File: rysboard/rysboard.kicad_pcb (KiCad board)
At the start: 4 copper layers, 56 x 65 mm, 150 parts, among them IC1 LM74801QDRRRQ1, IC2 LM74801QDRRRQ1, J1 RPi4, J10 ToF1, J11 ToF2, J12 ToF3, J13 ToF4, J15 ToF5, J16 ToF6, J19 Fan_Connector, J2 Motor L, J20 Power_SW, J22 CH1_T, J23 CH2_T, J3 Motor R, J4 Cell3, J5 Cell2, J6 Cell1, J7 Conn_01x02, J9 IMU, Q1 PMV28XPEAR, Q10 PMV28XPEAR, Q11 PMV28XPEAR, Q2 FDG6304P, Q3 NST847BDP6T5G, Q5 DMP3036SSD-13, Q6 Si7938DP-T1-GE3, Q7 NST847BDP6T5G, Q9 Si7938DP-T1-GE3, U1 L6470, U2 L6470, U3 ST1S10, U4 STM32G031K8Ux, U5 74HC2G00, U6 AP7381-33SA-7, U7 AP7381-33SA-7, U9 INA181

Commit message: layers stiched
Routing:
- net GND: vias 10 -> 210
- added copper zone on In1.Cu, net GND

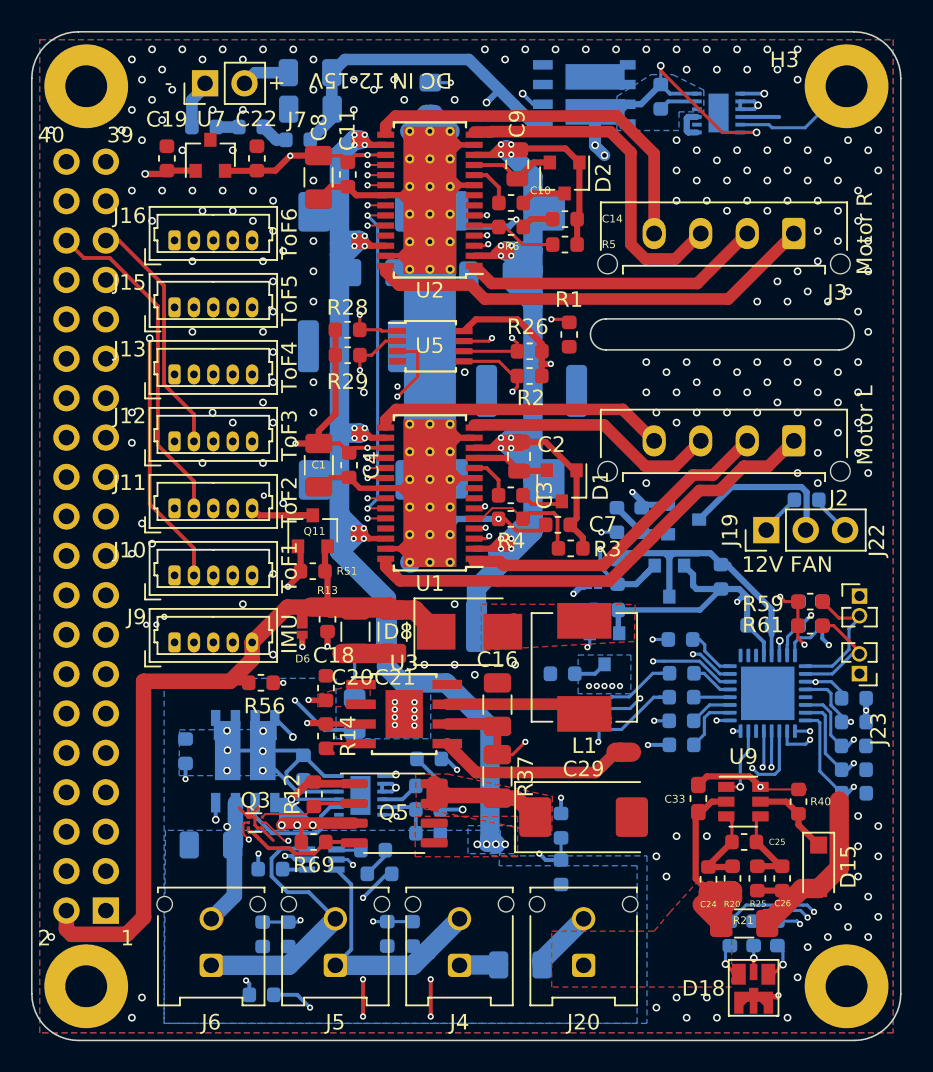
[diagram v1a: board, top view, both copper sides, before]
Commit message: Fixed regulator footprint
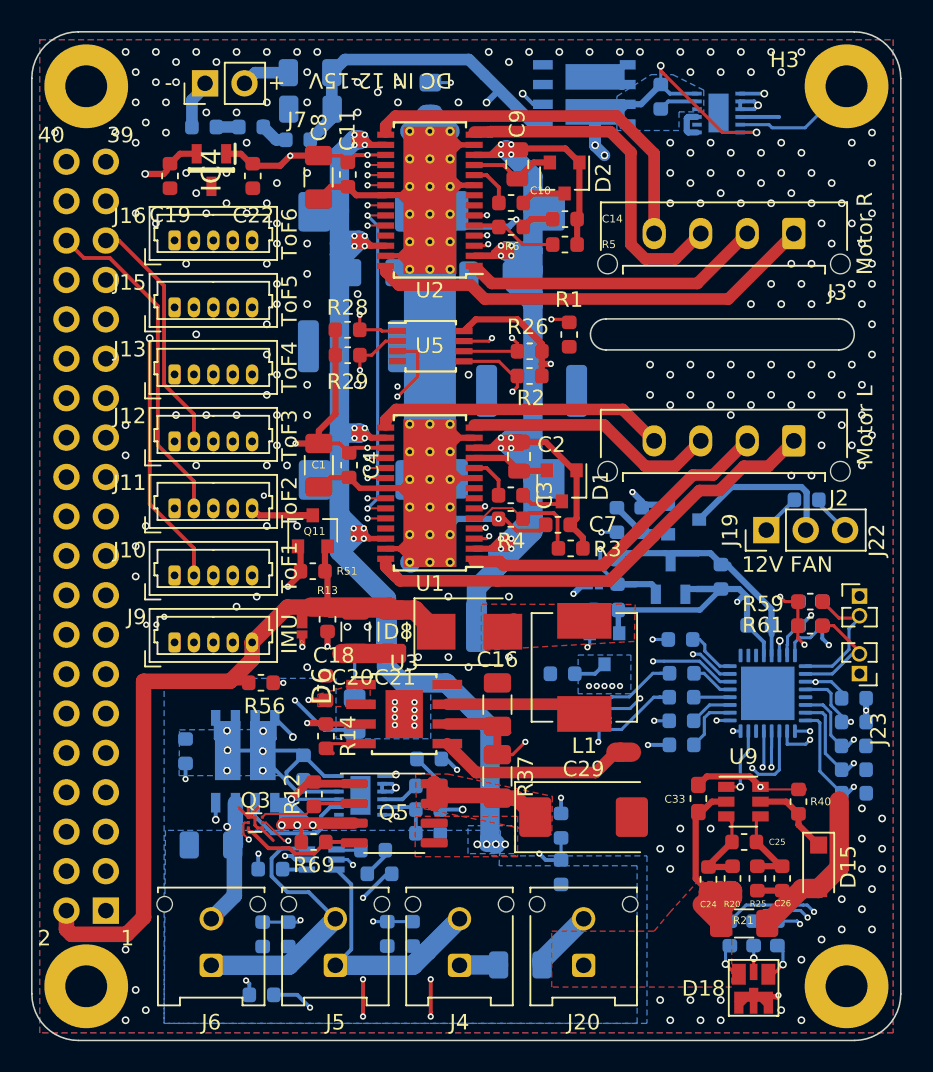
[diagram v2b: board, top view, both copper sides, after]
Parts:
- removed U6, U7: AP7381-33SA-7, Package_TO_SOT_SMD:SOT-23
- added IC3: MCP1812AT-033_TT, SOT95P237X112-3N, B.Cu at (116.5, 100.8)
- added IC4: MCP1812AT-033_TT, SOT95P237X112-3N, F.Cu at (86.9, 74.5)
- D5, D6: footprint SamacSys_Parts:DSN2_1 -> DSN2_1
- moved C22 1.16 mm to (89.5, 74.9), turned to 270 degrees
- moved C19 1.15 mm to (84.2, 74.9), turned to 270 degrees
- moved D5 0.06 mm to (111.3, 101.2)
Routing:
- net GND: track 190.8 -> 187.9 mm, vias 210 -> 220

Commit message: added connector for switch
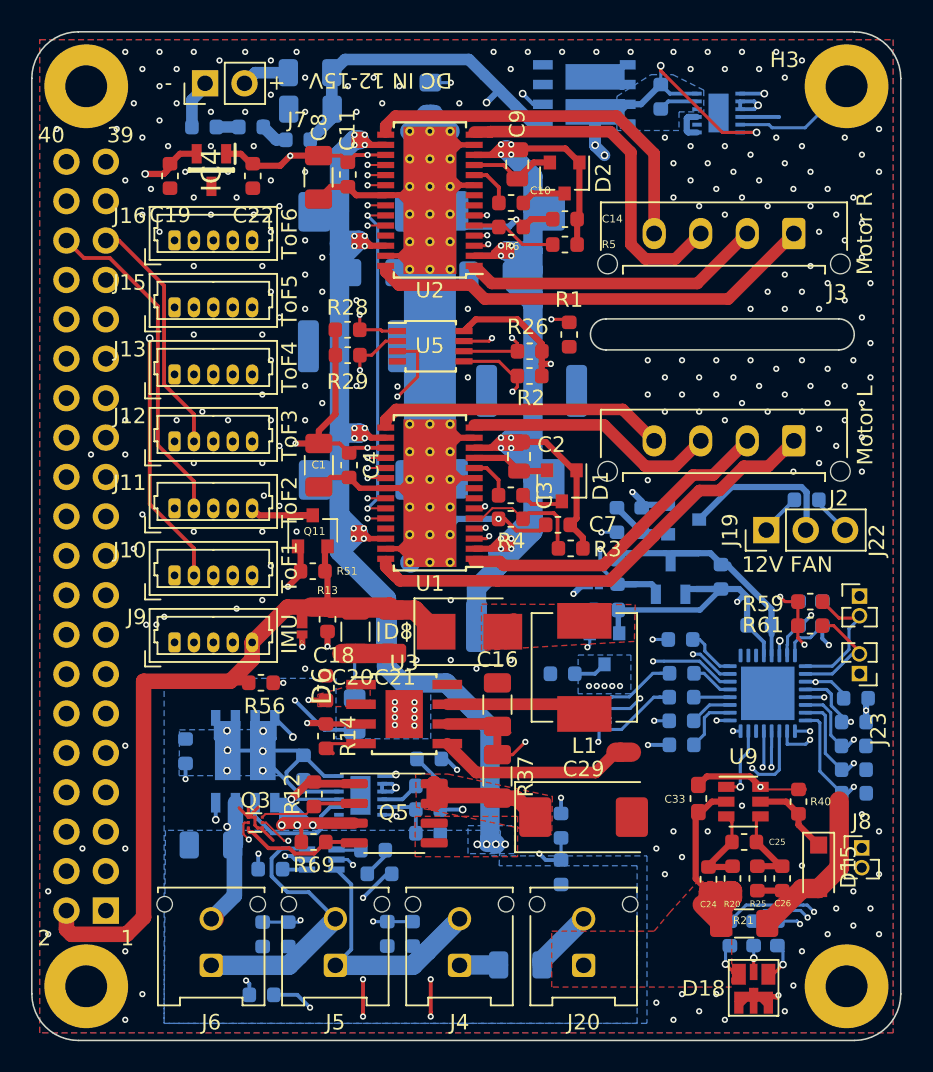
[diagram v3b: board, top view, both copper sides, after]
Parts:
- added J8: POWER SW, Connector_PinHeader_1.27mm:PinHeader_1x02_P1.27mm_Vertical, F.Cu at (128.8, 118.2)
- moved R55 0.13 mm to (128.4, 108.6)
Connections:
- U4 pad 13: /V_AUX -> /POWER_SW
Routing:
- net /POWER_SW: track 0.00 -> 15.0 mm, vias 0 -> 1
- net /BOARD_TEMP_PROBE_2: track 72.5 -> 76.3 mm
- net +5V: track 116.2 -> 117.0 mm
- net GND: vias 220 -> 226

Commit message: Bionik Logo added
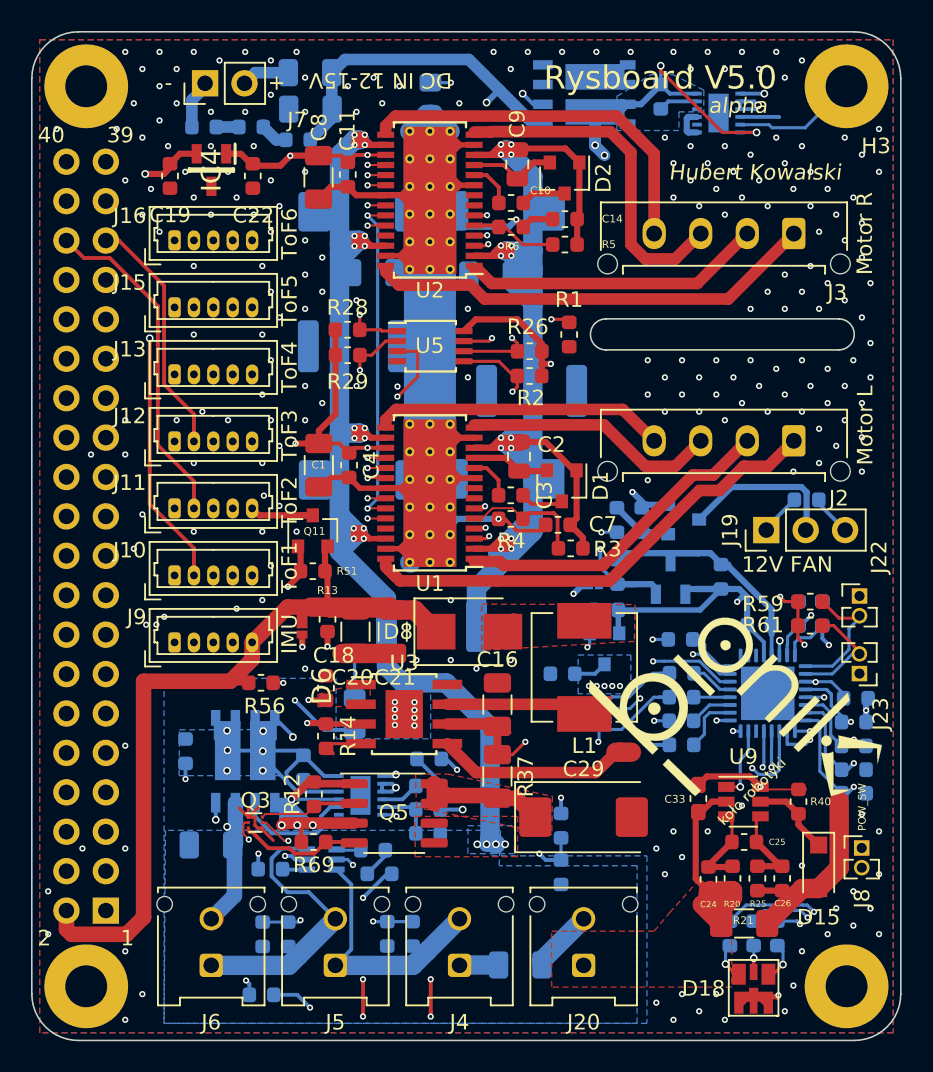
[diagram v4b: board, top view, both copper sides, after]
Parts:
- added LOGO1: bionik_logo, rysboard:bionik_logo, F.Cu at (120.6, 109.9)
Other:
- board text added: "Hubert Kowalski"
- board text added: "POW_SW"
- board text added: "Rysboard V5.0"
- board text added: "alpha"

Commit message: some acid pits fixed some ground problems fixed
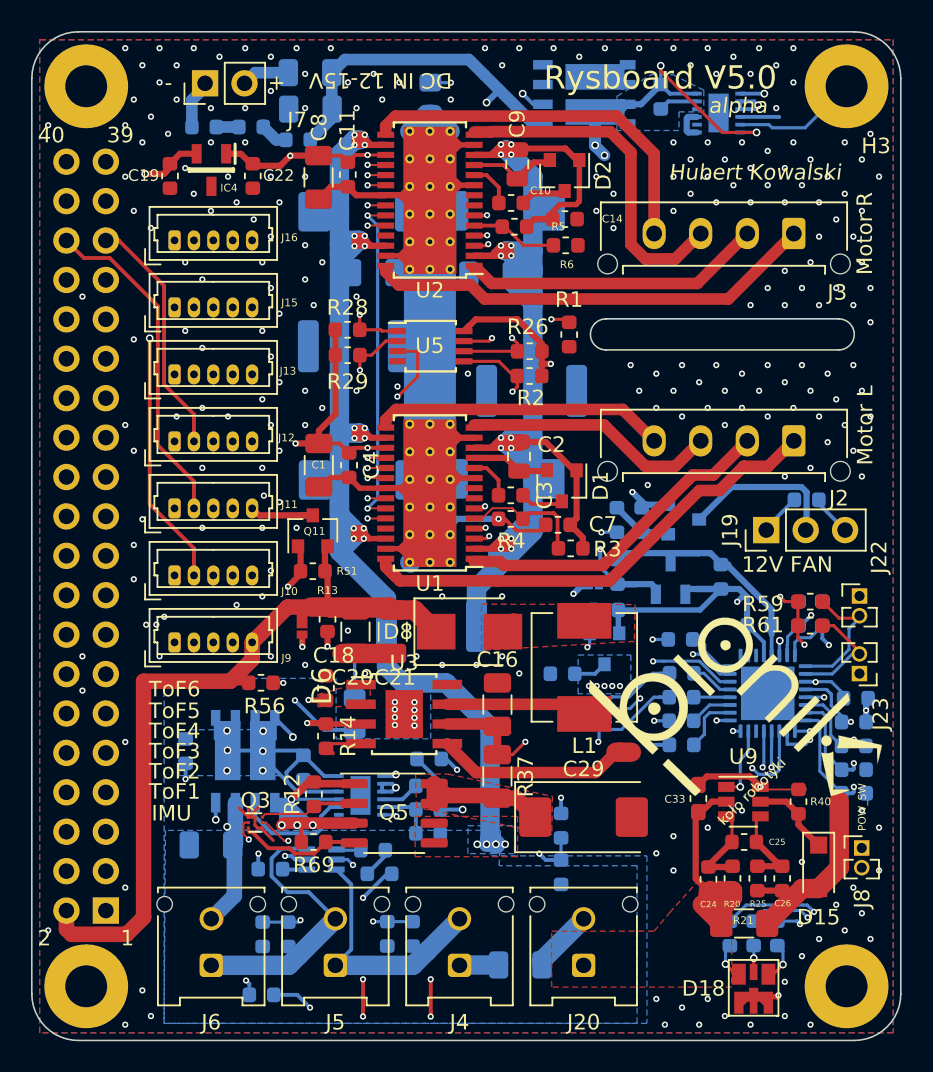
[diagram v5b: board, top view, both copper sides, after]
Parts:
- moved R6 3.71 mm to (109.7, 79.4)
- moved R5 3.45 mm to (106.4, 78.2)
- moved D2 0.16 mm to (109.6, 74.9)
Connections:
- C14 pad 1: Vdrive -> GND
- C14 pad 2: GND -> Vdrive
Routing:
- net GND: track 187.9 -> 181.7 mm, vias 226 -> 240
- net +BATT: track 72.1 -> 73.9 mm
- net Vdrive: track 214.9 -> 216.5 mm
- net /VBAT_2: track 57.8 -> 58.3 mm
- net /VBAT_3: track 61.2 -> 61.7 mm
- net /VBAT_1: track 53.2 -> 53.7 mm
